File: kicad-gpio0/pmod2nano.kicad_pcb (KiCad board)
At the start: 2 copper layers, 52 x 25 mm, 24 parts, among them J1 PMOD, J2 PMOD, J3 Conn_02x20_Odd_Even

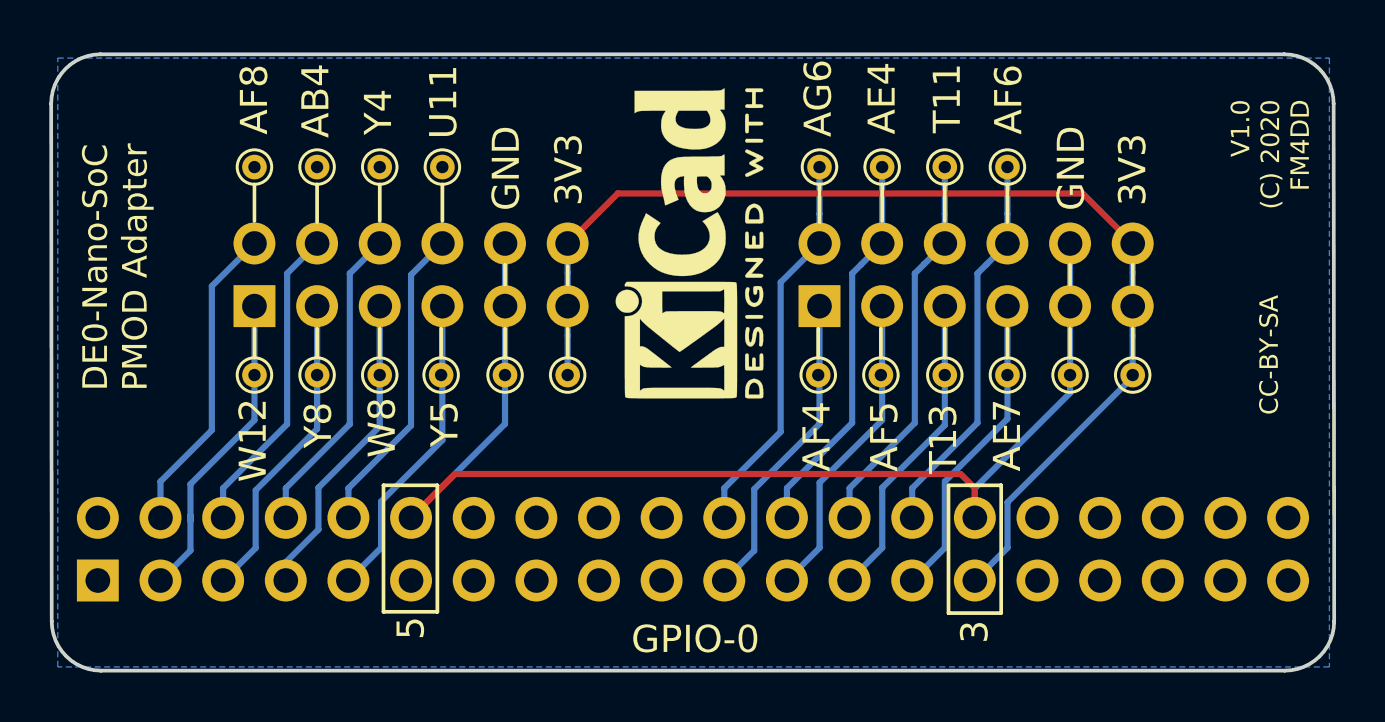
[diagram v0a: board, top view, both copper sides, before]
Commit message: testpin update gpio0
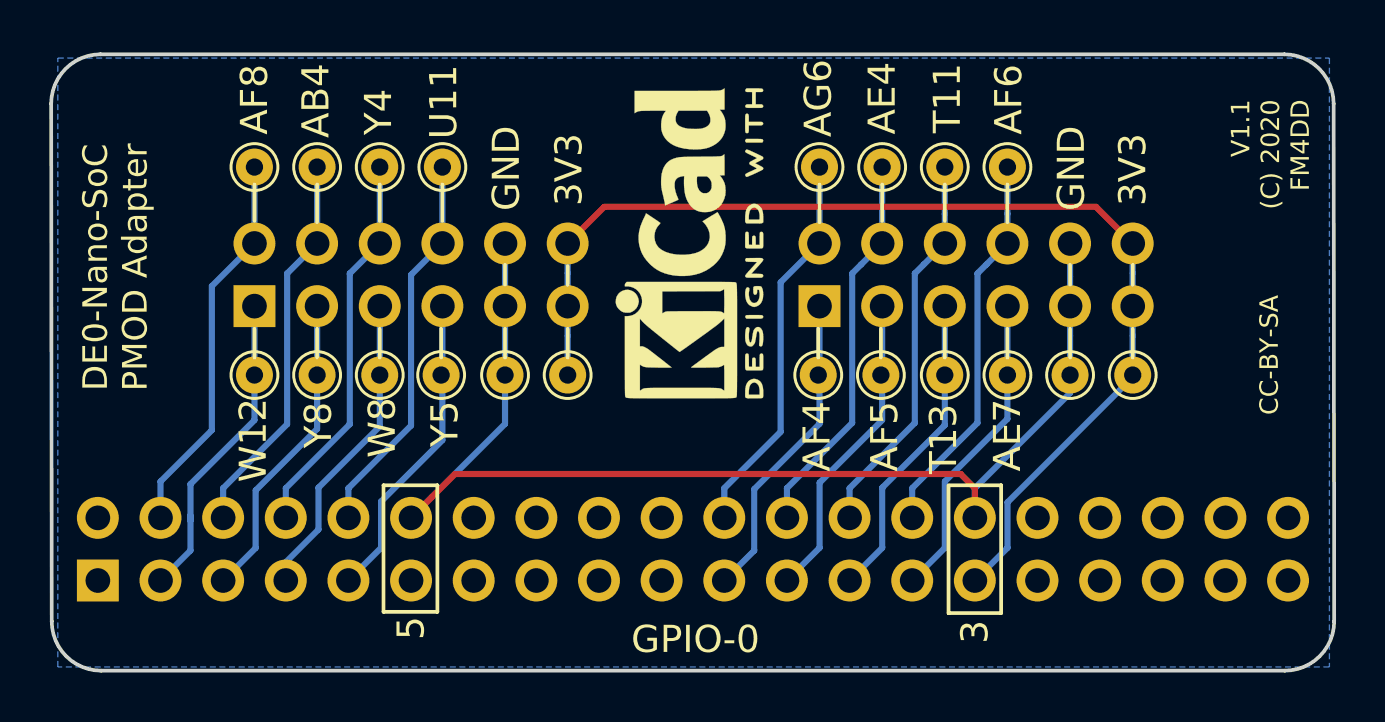
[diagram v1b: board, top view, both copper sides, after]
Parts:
- REF** (x20): value TestPoint_THTPad_D1.0mm_Drill0.5mm -> TestPoint_THTPad_D1.5mm_Drill0.7mm; footprint TestPoint:TestPoint_THTPad_D1.0mm_Drill0.5mm -> TestPoint:TestPoint_THTPad_D1.5mm_Drill0.7mm
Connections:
- REF** pad 1: (no net) -> /PIN_AF8
- REF** pad 1: (no net) -> /PIN_AB4
- REF** pad 1: (no net) -> /PIN_Y4
- REF** pad 1: (no net) -> /PIN_U11
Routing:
- net /PIN_Y4: track 12.7 -> 15.8 mm
- net /PIN_U11: track 12.7 -> 15.8 mm
- net /PIN_AF8: track 12.7 -> 15.8 mm
- net /PIN_AB4: track 12.7 -> 15.8 mm
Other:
- net class Default: clearance 0.24 -> 0.2
- rule trace_clearance: 0.24 -> 0.2
- board text added: "V1.1 (C) 2020 FM4DD"
- board text removed: "V1.0 (C) 2020 FM4DD"
